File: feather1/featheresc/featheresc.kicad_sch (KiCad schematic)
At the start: 10 parts, among them J1 VIN_GND, J2 VIN_POS, J7 interconnect1, J8 interconnect2

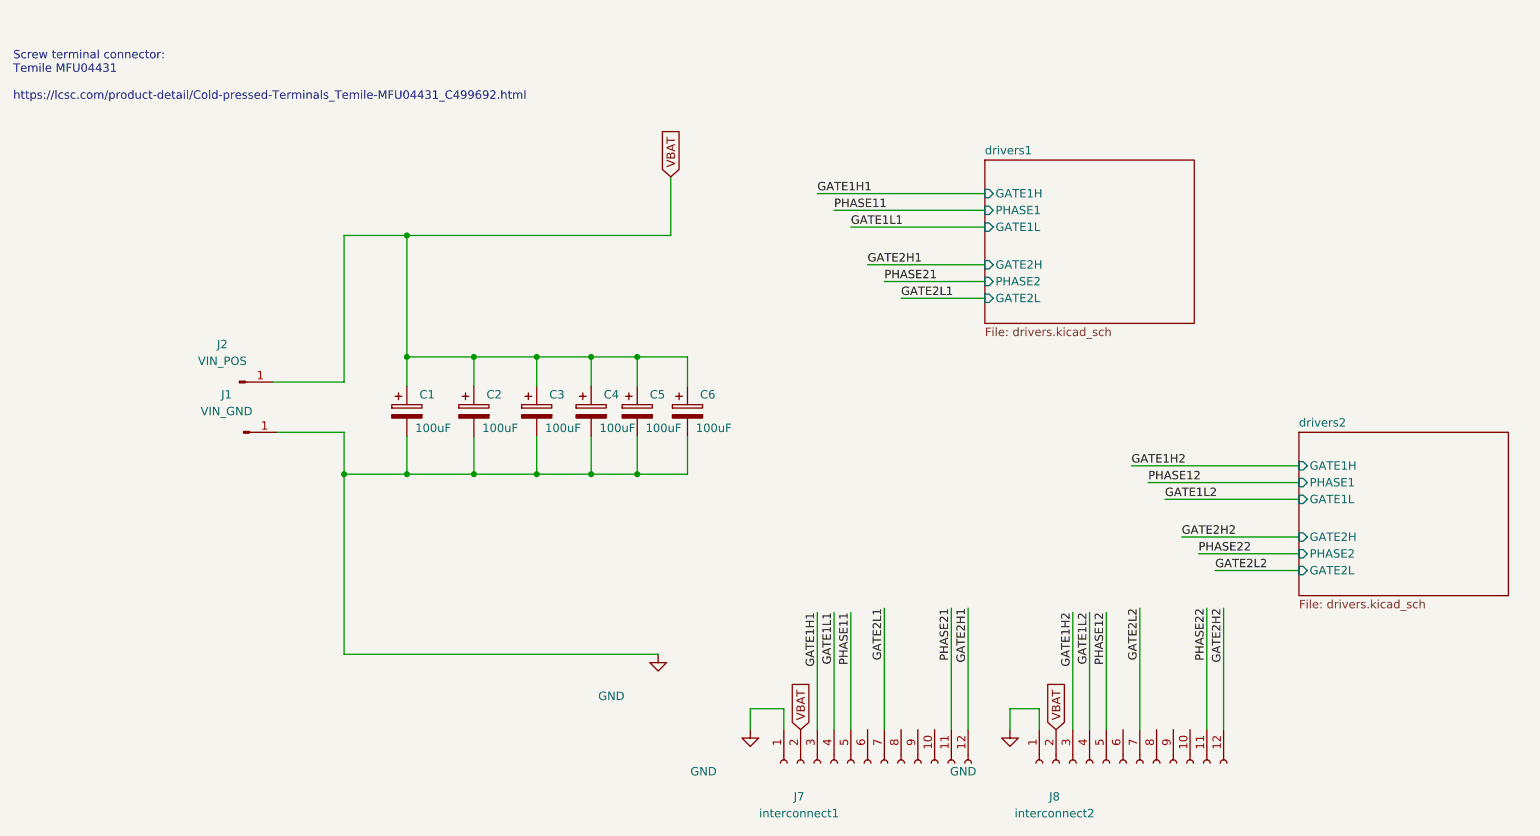
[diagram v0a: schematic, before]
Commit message: Feather ESC power board
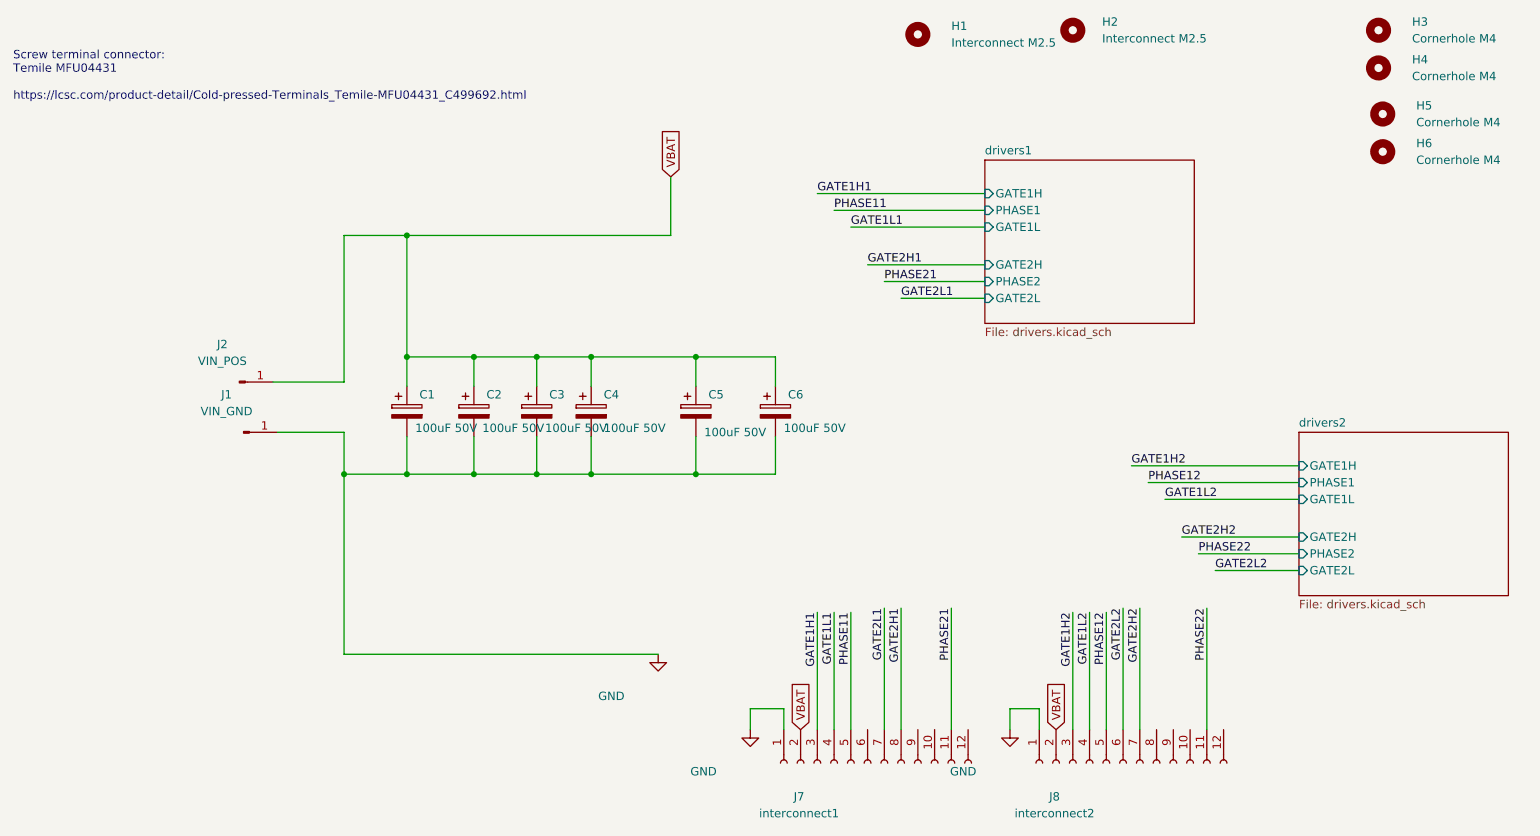
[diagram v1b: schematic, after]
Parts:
- added H1, H2: Interconnect M2.5, MountingHole:MountingHole_2.7mm_M2.5, symbol Mechanical:MountingHole
- added H3, H4, H5, H6: Cornerhole M4, MountingHole:MountingHole_4.3mm_M4, symbol Mechanical:MountingHole
- C1, C2, C3, C4, C5, C6: value 100uF -> 100uF 50V; footprint (none) -> Capacitor_SMD:CP_Elec_8x10; MPN (none) -> UUD1H101MNL1GS; Manufacturer (none) -> Nichicon
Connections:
- net GATE2H1: now also J7.8 (Pin_8); no longer J7.12 (Pin_12)
- net GATE2H2: now also J8.7 (Pin_7); no longer J8.12 (Pin_12)
- net GATE2L2: now also J8.6 (Pin_6); no longer J8.7 (Pin_7)
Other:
- moved on the sheet: C5, C6
